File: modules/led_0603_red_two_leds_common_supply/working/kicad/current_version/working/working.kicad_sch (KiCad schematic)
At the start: 4 parts

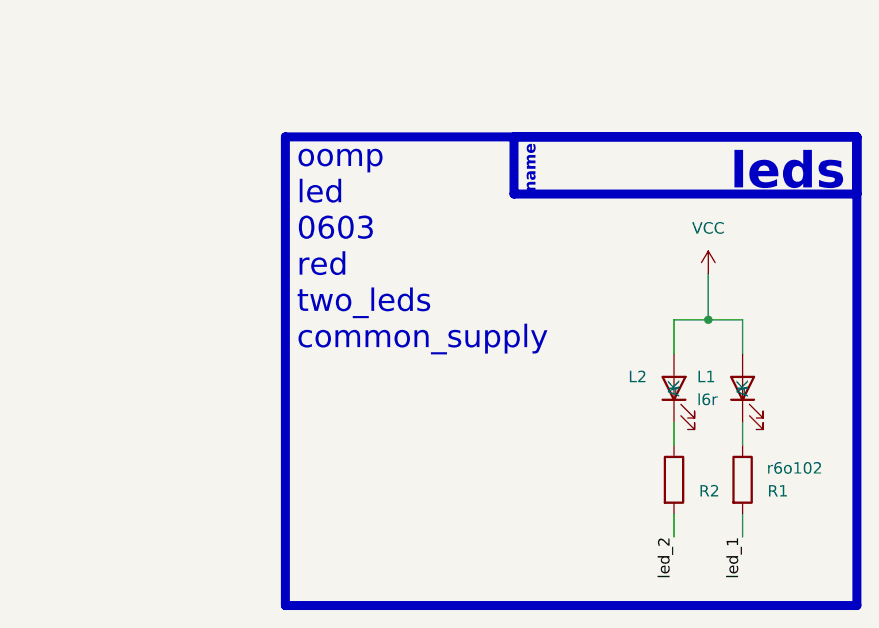
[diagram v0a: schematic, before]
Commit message: fixed formatting to be more consistent
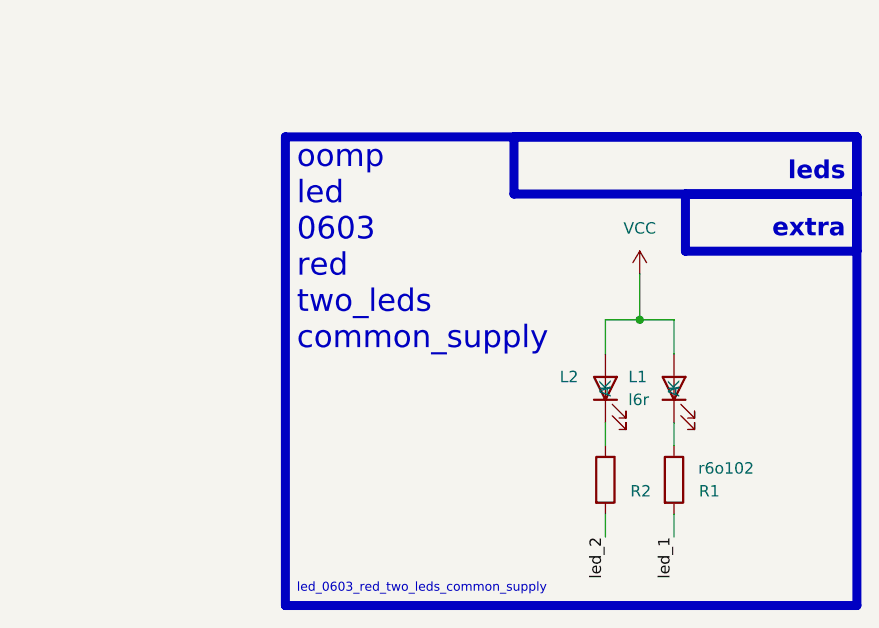
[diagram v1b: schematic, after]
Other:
- note added: "extra"
- note added: "led_0603_red_two_leds_common_supply"
- note removed: "name"
- moved on the sheet: L1, L2, R1, R2
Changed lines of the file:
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@@
 (kicad_sch (version 20230121) (generator eeschema)
   (paper "A4")
-  (junction (at 149.86 77.47) (diameter 0) (color 0 0 0 0)
+  (junction (at 142.24 77.47) (diameter 0) (color 0 0 0 0)
   )
-  (wire (pts (xy 146.05 101.6) (xy 146.05 99.06))
-    (stroke (width 0) (type default))
-  )
-  (wire (pts (xy 153.67 91.44) (xy 153.67 88.9))
-    (stroke (width 0) (type default))
-  )
-  (wire (pts (xy 149.86 77.47) (xy 149.86 72.39))
-    (stroke (width 0) (type default))
-  )
-  (wire (pts (xy 153.67 81.28) (xy 153.67 77.47))
-    (stroke (width 0) (type default))
-  )
-  (wire (pts (xy 153.67 101.6) (xy 153.67 99.06))
+  (wire (pts (xy 138.43 101.6) (xy 138.43 99.06))
     (stroke (width 0) (type default))
   )
@@
     (stroke (width 0) (type default))
   )
-  (wire (pts (xy 153.67 77.47) (xy 149.86 77.47))
+  (wire (pts (xy 142.24 77.47) (xy 142.24 72.39))
     (stroke (width 0) (type default))
   )
@@
     (stroke (width 0) (type default))
   )
-  (wire (pts (xy 149.86 77.47) (xy 146.05 77.47))
+  (wire (pts (xy 146.05 101.6) (xy 146.05 99.06))
+    (stroke (width 0) (type default))
+  )
+  (wire (pts (xy 138.43 91.44) (xy 138.43 88.9))
+    (stroke (width 0) (type default))
+  )
+  (wire (pts (xy 146.05 77.47) (xy 142.24 77.47))
+    (stroke (width 0) (type default))
+  )
+  (wire (pts (xy 138.43 81.28) (xy 138.43 77.47))
+    (stroke (width 0) (type default))
+  )
+  (wire (pts (xy 142.24 77.47) (xy 138.43 77.47))
     (stroke (width 0) (type default))
   )
   (rectangle (start 128.27 57.15) (end 166.37 63.5)
     (stroke (width 1) (type default))
-    (fill (type color) (color 0 0 0 0))
+    (fill (type none))
+  )
+  (rectangle (start 147.32 63.5) (end 166.37 69.85)
+    (stroke (width 1) (type default))
+    (fill (type none))
   )
   (rectangle (start 165.1 114.3) (end 165.1 114.3)
@@
     (fill (type none))
   )
-  (text "leds" (at 165.1 63.5 0)
-    (effects (font (size 4 4) (thickness 0.8) bold (color 255 255 255 1)) (justify right bottom))
+  (text "leds" (at 165.1 62.23 0)
+    (effects (font (size 2 2) (thickness 0.8) bold) (justify right bottom))
   )
   (text "oomp\nled\n0603\nred\ntwo_leds\ncommon_supply\n\n" (at 104.14 85.09 0)
     (effects (font (size 2.5 2.5)) (justify left bottom))
   )
-  (text "name" (at 130.81 63.5 90)
-    (effects (font (size 1.27 1.27) (thickness 0.254) bold (color 255 255 255 1)) (justify left bottom))
+  (text "extra" (at 165.1 68.58 0)
+    (effects (font (size 2 2) (thickness 0.8) bold) (justify right bottom))
   )
-  (label "led_1" (at 153.67 101.6 270) (fields_autoplaced)
+  (text "led_0603_red_two_leds_common_supply" (at 104.14 107.95 0)
+    (effects (font (size 1 1)) (justify left bottom))
+  )
+  (label "led_1" (at 146.05 101.6 270) (fields_autoplaced)
     (effects (font (size 1.27 1.27)) (justify right bottom))
   )
-  (label "led_2" (at 146.05 101.6 270) (fields_autoplaced)
+  (label "led_2" (at 138.43 101.6 270) (fields_autoplaced)
     (effects (font (size 1.27 1.27)) (justify right bottom))
   )
-  (symbol (lib_id "oomlout_oomp_part_symbols:r6o102_electronic_resistor_0603_1000_ohm") (at 153.67 95.25 0) (unit 1)
+  (symbol (lib_id "oomlout_oomp_part_symbols:r6o102_electronic_resistor_0603_1000_ohm") (at 146.05 95.25 0) (unit 1)
     (in_bom yes) (on_board yes) (dnp no)
-    (property "Reference" "R1" (at 158.75 96.52 0)
+    (property "Reference" "R1" (at 151.13 96.52 0)
       (effects (font (size 1.27 1.27)) (justify right))
     )
-    (property "Value" "r6o102" (at 162.56 93.98 0)
+    (property "Value" "r6o102" (at 154.94 93.98 0)
       (effects (font (size 1.27 1.27)) (justify right))
     )
-    (property "Footprint" "r6o102_electronic_resistor_0603_1000_ohm" (at 151.892 95.25 90)
+    (property "Footprint" "r6o102_electronic_resistor_0603_1000_ohm" (at 144.272 95.25 90)
       (effects (font (size 1.27 1.27)) hide)
     )
-    (property "Datasheet" "https://github.com/oomlout/oomlout_oomp_v3/parts/electronic_resistor_0603_1000_ohm/datasheet.pdf" (at 153.67 95.25 0)
+    (property "Datasheet" "https://github.com/oomlout/oomlout_oomp_v3/parts/electronic_resistor_0603_1000_ohm/datasheet.pdf" (at 146.05 95.25 0)
       (effects (font (size 1.27 1.27)) hide)
     )
@@
     )
   )
+  (symbol (lib_id "oomlout_oomp_part_symbols:l6r_electronic_led_0603_red") (at 138.43 85.09 90) (unit 1)
+    (in_bom yes) (on_board yes) (dnp no)
+    (property "Reference" "L2" (at 133.35 83.82 90)
+      (effects (font (size 1.27 1.27)) (justify right))
+    )
+    (property "Value" "l6r" (at 133.35 86.36 90)
+      (effects (font (size 1.27 1.27)) (justify right) hide)
+    )
+    (property "Footprint" "l6r_electronic_led_0603_red" (at 138.43 85.09 0)
+      (effects (font (size 1.27 1.27)) hide)
+    )
+    (property "Datasheet" "https://github.com/oomlout/oomlout_oomp_v3/parts/electronic_led_0603_red/datasheet.pdf" (at 138.43 85.09 0)
+      (effects (font (size 1.27 1.27)) hide)
+    )
+    (pin "1")
+    (pin "2")
+    (instances
+      (project "working"
+        (path "/34a6fca3-0155-4091-9a11-9123c8ad4011"
+          (reference "L2") (unit 1)
+        )
+      )
+    )
+  )
   (symbol (lib_id "oomlout_oomp_part_symbols:l6r_electronic_led_0603_red") (at 146.05 85.09 90) (unit 1)
     (in_bom yes) (on_board yes) (dnp no)
-    (property "Reference" "L2" (at 140.97 83.82 90)
+    (property "Reference" "L1" (at 140.97 83.82 90)
       (effects (font (size 1.27 1.27)) (justify right))
     )
     (property "Value" "l6r" (at 140.97 86.36 90)
-      (effects (font (size 1.27 1.27)) (justify right) hide)
+      (effects (font (size 1.27 1.27)) (justify right))
     )
     (property "Footprint" "l6r_electronic_led_0603_red" (at 146.05 85.09 0)
@@
       (project "working"
         (path "/34a6fca3-0155-4091-9a11-9123c8ad4011"
-          (reference "L2") (unit 1)
-        )
-      )
-    )
-  )
-  (symbol (lib_id "oomlout_oomp_part_symbols:l6r_electronic_led_0603_red") (at 153.67 85.09 90) (unit 1)
-    (in_bom yes) (on_board yes) (dnp no)
-    (property "Reference" "L1" (at 148.59 83.82 90)
-      (effects (font (size 1.27 1.27)) (justify right))
-    )
-    (property "Value" "l6r" (at 148.59 86.36 90)
-      (effects (font (size 1.27 1.27)) (justify right))
-    )
-    (property "Footprint" "l6r_electronic_led_0603_red" (at 153.67 85.09 0)
-      (effects (font (size 1.27 1.27)) hide)
-    )
-    (property "Datasheet" "https://github.com/oomlout/oomlout_oomp_v3/parts/electronic_led_0603_red/datasheet.pdf" (at 153.67 85.09 0)
-      (effects (font (size 1.27 1.27)) hide)
-    )
-    (pin "1")
-    (pin "2")
-    (instances
-      (project "working"
-        (path "/34a6fca3-0155-4091-9a11-9123c8ad4011"
           (reference "L1") (unit 1)
         )
@@
     )
   )
-  (symbol (lib_id "oomlout_oomp_part_symbols:r6o102_electronic_resistor_0603_1000_ohm") (at 146.05 95.25 0) (unit 1)
+  (symbol (lib_id "oomlout_oomp_part_symbols:r6o102_electronic_resistor_0603_1000_ohm") (at 138.43 95.25 0) (unit 1)
     (in_bom yes) (on_board yes) (dnp no)
-    (property "Reference" "R2" (at 151.13 96.52 0)
+    (property "Reference" "R2" (at 143.51 96.52 0)
       (effects (font (size 1.27 1.27)) (justify right))
     )
-    (property "Value" "r6o102" (at 154.94 93.98 0)
+    (property "Value" "r6o102" (at 147.32 93.98 0)
       (effects (font (size 1.27 1.27)) (justify right) hide)
     )
-    (property "Footprint" "r6o102_electronic_resistor_0603_1000_ohm" (at 144.272 95.25 90)
+    (property "Footprint" "r6o102_electronic_resistor_0603_1000_ohm" (at 136.652 95.25 90)
       (effects (font (size 1.27 1.27)) hide)
     )
-    (property "Datasheet" "https://github.com/oomlout/oomlout_oomp_v3/parts/electronic_resistor_0603_1000_ohm/datasheet.pdf" (at 146.05 95.25 0)
+    (property "Datasheet" "https://github.com/oomlout/oomlout_oomp_v3/parts/electronic_resistor_0603_1000_ohm/datasheet.pdf" (at 138.43 95.25 0)
       (effects (font (size 1.27 1.27)) hide)
     )
@@
     )
   )
-  (symbol (lib_id "power:VCC") (at 149.86 72.39 0) (unit 1)
+  (symbol (lib_id "power:VCC") (at 142.24 72.39 0) (unit 1)
     (in_bom yes) (on_board yes) (dnp no) (fields_autoplaced)
-    (property "Reference" "#PWR01" (at 149.86 76.2 0)
+    (property "Reference" "#PWR01" (at 142.24 76.2 0)
       (effects (font (size 1.27 1.27)) hide)
     )
-    (property "Value" "VCC" (at 149.86 67.31 0)
+    (property "Value" "VCC" (at 142.24 67.31 0)
       (effects (font (size 1.27 1.27)))
     )
-    (property "Footprint" "" (at 149.86 72.39 0)
+    (property "Footprint" "" (at 142.24 72.39 0)
       (effects (font (size 1.27 1.27)) hide)
     )
-    (property "Datasheet" "" (at 149.86 72.39 0)
+    (property "Datasheet" "" (at 142.24 72.39 0)
       (effects (font (size 1.27 1.27)) hide)
     )

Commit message: schematic formatting
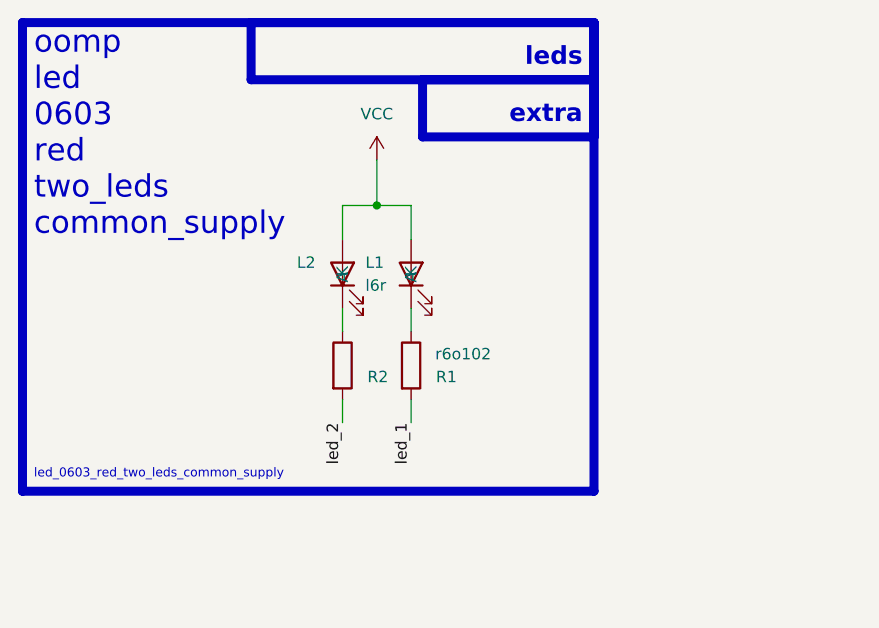
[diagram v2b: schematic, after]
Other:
- moved on the sheet: L1, L2, R1, R2
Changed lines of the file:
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@@
 (kicad_sch (version 20230121) (generator eeschema)
-  (paper "A4")
-  (junction (at 142.24 77.47) (diameter 0) (color 0 0 0 0)
+  (paper "A5")
+  (junction (at 113.03 64.77) (diameter 0) (color 0 0 0 0)
   )
-  (wire (pts (xy 138.43 101.6) (xy 138.43 99.06))
+  (wire (pts (xy 109.22 88.9) (xy 109.22 86.36))
     (stroke (width 0) (type default))
   )
-  (wire (pts (xy 146.05 91.44) (xy 146.05 88.9))
+  (wire (pts (xy 116.84 78.74) (xy 116.84 76.2))
     (stroke (width 0) (type default))
   )
-  (wire (pts (xy 142.24 77.47) (xy 142.24 72.39))
+  (wire (pts (xy 113.03 64.77) (xy 113.03 59.69))
     (stroke (width 0) (type default))
   )
-  (wire (pts (xy 146.05 81.28) (xy 146.05 77.47))
+  (wire (pts (xy 116.84 68.58) (xy 116.84 64.77))
     (stroke (width 0) (type default))
   )
-  (wire (pts (xy 146.05 101.6) (xy 146.05 99.06))
+  (wire (pts (xy 116.84 88.9) (xy 116.84 86.36))
     (stroke (width 0) (type default))
   )
-  (wire (pts (xy 138.43 91.44) (xy 138.43 88.9))
+  (wire (pts (xy 109.22 78.74) (xy 109.22 76.2))
     (stroke (width 0) (type default))
   )
-  (wire (pts (xy 146.05 77.47) (xy 142.24 77.47))
+  (wire (pts (xy 116.84 64.77) (xy 113.03 64.77))
     (stroke (width 0) (type default))
   )
-  (wire (pts (xy 138.43 81.28) (xy 138.43 77.47))
+  (wire (pts (xy 109.22 68.58) (xy 109.22 64.77))
     (stroke (width 0) (type default))
   )
-  (wire (pts (xy 142.24 77.47) (xy 138.43 77.47))
+  (wire (pts (xy 113.03 64.77) (xy 109.22 64.77))
     (stroke (width 0) (type default))
   )
-  (rectangle (start 128.27 57.15) (end 166.37 63.5)
+  (rectangle (start 99.06 44.45) (end 137.16 50.8)
     (stroke (width 1) (type default))
     (fill (type none))
   )
-  (rectangle (start 147.32 63.5) (end 166.37 69.85)
+  (rectangle (start 118.11 50.8) (end 137.16 57.15)
     (stroke (width 1) (type default))
     (fill (type none))
   )
-  (rectangle (start 165.1 114.3) (end 165.1 114.3)
+  (rectangle (start 135.89 101.6) (end 135.89 101.6)
     (stroke (width 0) (type default))
     (fill (type none))
   )
-  (rectangle (start 102.87 57.15) (end 166.37 109.22)
+  (rectangle (start 73.66 44.45) (end 137.16 96.52)
     (stroke (width 1) (type default))
     (fill (type none))
   )
-  (text "leds" (at 165.1 62.23 0)
+  (text "leds" (at 135.89 49.53 0)
     (effects (font (size 2 2) (thickness 0.8) bold) (justify right bottom))
   )
-  (text "oomp\nled\n0603\nred\ntwo_leds\ncommon_supply\n\n" (at 104.14 85.09 0)
+  (text "oomp\nled\n0603\nred\ntwo_leds\ncommon_supply\n\n" (at 74.93 72.39 0)
     (effects (font (size 2.5 2.5)) (justify left bottom))
   )
-  (text "extra" (at 165.1 68.58 0)
+  (text "extra" (at 135.89 55.88 0)
     (effects (font (size 2 2) (thickness 0.8) bold) (justify right bottom))
   )
-  (text "led_0603_red_two_leds_common_supply" (at 104.14 107.95 0)
+  (text "led_0603_red_two_leds_common_supply" (at 74.93 95.25 0)
     (effects (font (size 1 1)) (justify left bottom))
   )
-  (label "led_1" (at 146.05 101.6 270) (fields_autoplaced)
+  (label "led_1" (at 116.84 88.9 270) (fields_autoplaced)
     (effects (font (size 1.27 1.27)) (justify right bottom))
   )
-  (label "led_2" (at 138.43 101.6 270) (fields_autoplaced)
+  (label "led_2" (at 109.22 88.9 270) (fields_autoplaced)
     (effects (font (size 1.27 1.27)) (justify right bottom))
   )
-  (symbol (lib_id "oomlout_oomp_part_symbols:r6o102_electronic_resistor_0603_1000_ohm") (at 146.05 95.25 0) (unit 1)
+  (symbol (lib_id "oomlout_oomp_part_symbols:r6o102_electronic_resistor_0603_1000_ohm") (at 116.84 82.55 0) (unit 1)
     (in_bom yes) (on_board yes) (dnp no)
-    (property "Reference" "R1" (at 151.13 96.52 0)
+    (property "Reference" "R1" (at 121.92 83.82 0)
       (effects (font (size 1.27 1.27)) (justify right))
     )
-    (property "Value" "r6o102" (at 154.94 93.98 0)
+    (property "Value" "r6o102" (at 125.73 81.28 0)
       (effects (font (size 1.27 1.27)) (justify right))
     )
-    (property "Footprint" "r6o102_electronic_resistor_0603_1000_ohm" (at 144.272 95.25 90)
+    (property "Footprint" "r6o102_electronic_resistor_0603_1000_ohm" (at 115.062 82.55 90)
       (effects (font (size 1.27 1.27)) hide)
     )
-    (property "Datasheet" "https://github.com/oomlout/oomlout_oomp_v3/parts/electronic_resistor_0603_1000_ohm/datasheet.pdf" (at 146.05 95.25 0)
+    (property "Datasheet" "https://github.com/oomlout/oomlout_oomp_v3/parts/electronic_resistor_0603_1000_ohm/datasheet.pdf" (at 116.84 82.55 0)
       (effects (font (size 1.27 1.27)) hide)
     )
@@
     )
   )
-  (symbol (lib_id "oomlout_oomp_part_symbols:l6r_electronic_led_0603_red") (at 138.43 85.09 90) (unit 1)
+  (symbol (lib_id "oomlout_oomp_part_symbols:l6r_electronic_led_0603_red") (at 109.22 72.39 90) (unit 1)
     (in_bom yes) (on_board yes) (dnp no)
-    (property "Reference" "L2" (at 133.35 83.82 90)
+    (property "Reference" "L2" (at 104.14 71.12 90)
       (effects (font (size 1.27 1.27)) (justify right))
     )
-    (property "Value" "l6r" (at 133.35 86.36 90)
+    (property "Value" "l6r" (at 104.14 73.66 90)
       (effects (font (size 1.27 1.27)) (justify right) hide)
     )
-    (property "Footprint" "l6r_electronic_led_0603_red" (at 138.43 85.09 0)
+    (property "Footprint" "l6r_electronic_led_0603_red" (at 109.22 72.39 0)
       (effects (font (size 1.27 1.27)) hide)
     )
-    (property "Datasheet" "https://github.com/oomlout/oomlout_oomp_v3/parts/electronic_led_0603_red/datasheet.pdf" (at 138.43 85.09 0)
+    (property "Datasheet" "https://github.com/oomlout/oomlout_oomp_v3/parts/electronic_led_0603_red/datasheet.pdf" (at 109.22 72.39 0)
       (effects (font (size 1.27 1.27)) hide)
     )
@@
     )
   )
-  (symbol (lib_id "oomlout_oomp_part_symbols:l6r_electronic_led_0603_red") (at 146.05 85.09 90) (unit 1)
+  (symbol (lib_id "oomlout_oomp_part_symbols:l6r_electronic_led_0603_red") (at 116.84 72.39 90) (unit 1)
     (in_bom yes) (on_board yes) (dnp no)
-    (property "Reference" "L1" (at 140.97 83.82 90)
+    (property "Reference" "L1" (at 111.76 71.12 90)
       (effects (font (size 1.27 1.27)) (justify right))
     )
-    (property "Value" "l6r" (at 140.97 86.36 90)
+    (property "Value" "l6r" (at 111.76 73.66 90)
       (effects (font (size 1.27 1.27)) (justify right))
     )
-    (property "Footprint" "l6r_electronic_led_0603_red" (at 146.05 85.09 0)
+    (property "Footprint" "l6r_electronic_led_0603_red" (at 116.84 72.39 0)
       (effects (font (size 1.27 1.27)) hide)
     )
-    (property "Datasheet" "https://github.com/oomlout/oomlout_oomp_v3/parts/electronic_led_0603_red/datasheet.pdf" (at 146.05 85.09 0)
+    (property "Datasheet" "https://github.com/oomlout/oomlout_oomp_v3/parts/electronic_led_0603_red/datasheet.pdf" (at 116.84 72.39 0)
       (effects (font (size 1.27 1.27)) hide)
     )
@@
     )
   )
-  (symbol (lib_id "oomlout_oomp_part_symbols:r6o102_electronic_resistor_0603_1000_ohm") (at 138.43 95.25 0) (unit 1)
+  (symbol (lib_id "oomlout_oomp_part_symbols:r6o102_electronic_resistor_0603_1000_ohm") (at 109.22 82.55 0) (unit 1)
     (in_bom yes) (on_board yes) (dnp no)
-    (property "Reference" "R2" (at 143.51 96.52 0)
+    (property "Reference" "R2" (at 114.3 83.82 0)
       (effects (font (size 1.27 1.27)) (justify right))
     )
-    (property "Value" "r6o102" (at 147.32 93.98 0)
+    (property "Value" "r6o102" (at 118.11 81.28 0)
       (effects (font (size 1.27 1.27)) (justify right) hide)
     )
-    (property "Footprint" "r6o102_electronic_resistor_0603_1000_ohm" (at 136.652 95.25 90)
+    (property "Footprint" "r6o102_electronic_resistor_0603_1000_ohm" (at 107.442 82.55 90)
       (effects (font (size 1.27 1.27)) hide)
     )
-    (property "Datasheet" "https://github.com/oomlout/oomlout_oomp_v3/parts/electronic_resistor_0603_1000_ohm/datasheet.pdf" (at 138.43 95.25 0)
+    (property "Datasheet" "https://github.com/oomlout/oomlout_oomp_v3/parts/electronic_resistor_0603_1000_ohm/datasheet.pdf" (at 109.22 82.55 0)
       (effects (font (size 1.27 1.27)) hide)
     )
@@
     )
   )
-  (symbol (lib_id "power:VCC") (at 142.24 72.39 0) (unit 1)
+  (symbol (lib_id "power:VCC") (at 113.03 59.69 0) (unit 1)
     (in_bom yes) (on_board yes) (dnp no) (fields_autoplaced)
-    (property "Reference" "#PWR01" (at 142.24 76.2 0)
+    (property "Reference" "#PWR01" (at 113.03 63.5 0)
       (effects (font (size 1.27 1.27)) hide)
     )
-    (property "Value" "VCC" (at 142.24 67.31 0)
+    (property "Value" "VCC" (at 113.03 54.61 0)
       (effects (font (size 1.27 1.27)))
     )
-    (property "Footprint" "" (at 142.24 72.39 0)
+    (property "Footprint" "" (at 113.03 59.69 0)
       (effects (font (size 1.27 1.27)) hide)
     )
-    (property "Datasheet" "" (at 142.24 72.39 0)
+    (property "Datasheet" "" (at 113.03 59.69 0)
       (effects (font (size 1.27 1.27)) hide)
     )
